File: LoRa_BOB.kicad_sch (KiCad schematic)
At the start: 8 parts, among them U1 1597-1488-ND, U2 XC6210B332MR-G, U3 74HC4050D

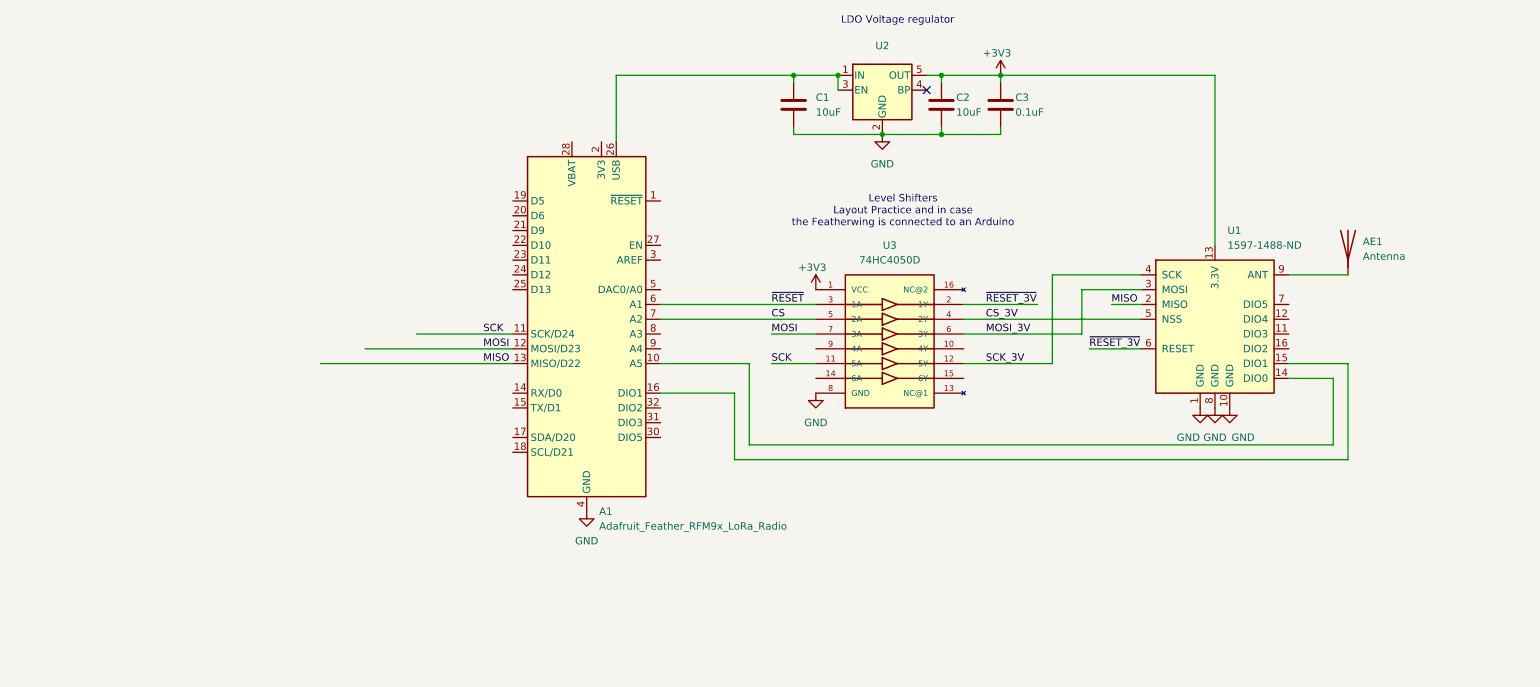
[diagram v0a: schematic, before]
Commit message: netclass directive cleanup
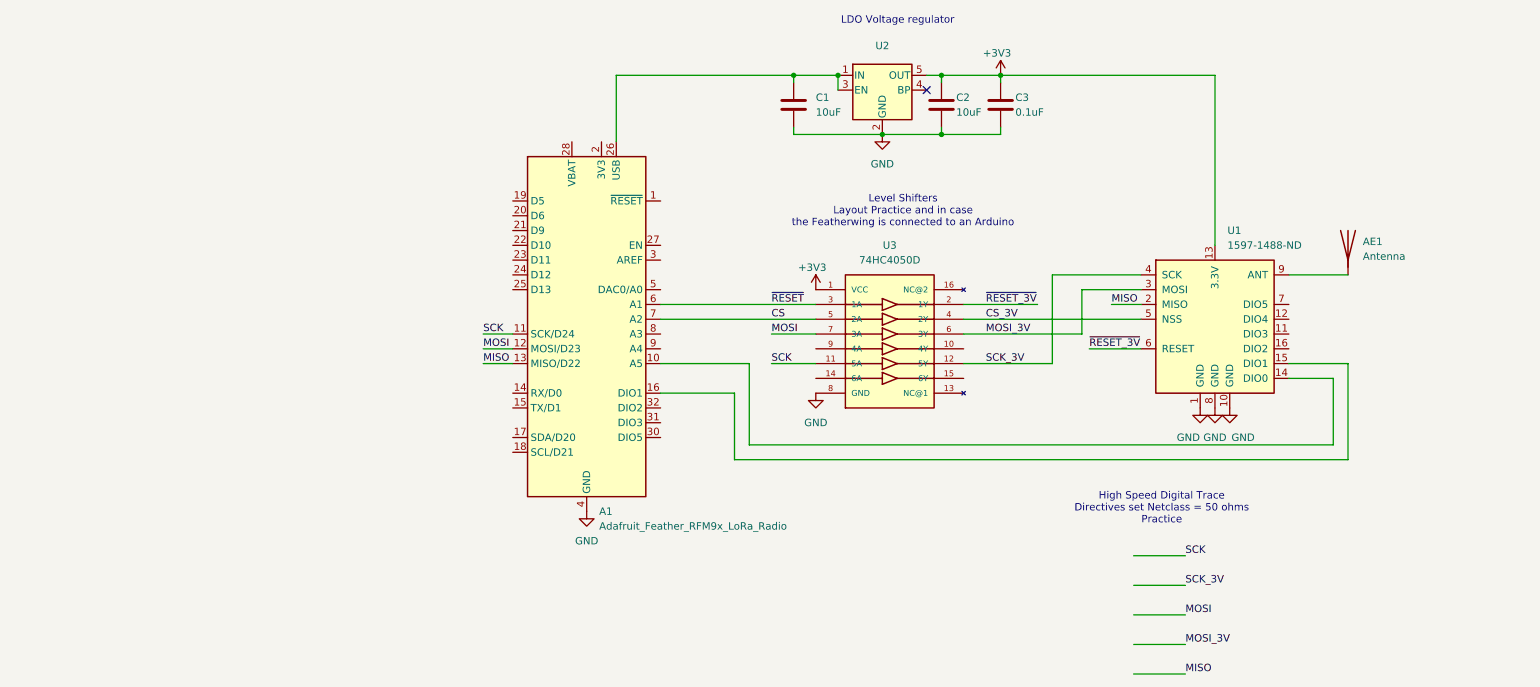
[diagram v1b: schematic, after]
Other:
- note added: "High Speed Digital Trace Directives set Netclass = 50 ohms Practice"
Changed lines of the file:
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@@
+		)
+	)
+	(text "High Speed Digital Trace\nDirectives set Netclass = 50 ohms\nPractice"
+		(exclude_from_sim no)
+		(at 270.256 154.432 0)
+		(effects
+			(font
+				(size 1.27 1.27)
+			)
 		)
 	)
@@
 	(wire
 		(pts
-			(xy 125.73 129.54) (xy 158.75 129.54)
+			(xy 153.67 124.46) (xy 158.75 124.46)
 		)
 		(stroke
@@
 	(wire
 		(pts
+			(xy 153.67 127) (xy 158.75 127)
+		)
+		(stroke
+			(width 0)
+			(type default)
+		)
+	)
+	(wire
+		(pts
 			(xy 299.72 143.51) (xy 299.72 132.08)
 		)
@@
 	(wire
 		(pts
-			(xy 133.35 127) (xy 158.75 127)
-		)
-		(stroke
-			(width 0)
-			(type default)
-		)
-	)
-	(wire
-		(pts
 			(xy 232.41 88.9) (xy 232.41 90.17)
 		)
@@
 	(wire
 		(pts
+			(xy 265.43 167.64) (xy 274.32 167.64)
+		)
+		(stroke
+			(width 0)
+			(type default)
+		)
+	)
+	(wire
+		(pts
 			(xy 242.57 90.17) (xy 232.41 90.17)
 		)
@@
 	(wire
 		(pts
+			(xy 265.43 172.72) (xy 274.32 172.72)
+		)
+		(stroke
+			(width 0)
+			(type default)
+		)
+	)
+	(wire
+		(pts
 			(xy 207.01 90.17) (xy 222.25 90.17)
 		)
@@
 	(wire
 		(pts
+			(xy 265.43 162.56) (xy 274.32 162.56)
+		)
+		(stroke
+			(width 0)
+			(type default)
+		)
+	)
+	(wire
+		(pts
 			(xy 236.22 119.38) (xy 248.92 119.38)
 		)
@@
 	(wire
 		(pts
+			(xy 153.67 129.54) (xy 158.75 129.54)
+		)
+		(stroke
+			(width 0)
+			(type default)
+		)
+	)
+	(wire
+		(pts
 			(xy 184.15 121.92) (xy 210.82 121.92)
 		)
@@
 	(wire
 		(pts
+			(xy 265.43 182.88) (xy 274.32 182.88)
+		)
+		(stroke
+			(width 0)
+			(type default)
+		)
+	)
+	(wire
+		(pts
 			(xy 176.53 91.44) (xy 176.53 80.01)
 		)
@@
 	(wire
 		(pts
-			(xy 142.24 124.46) (xy 158.75 124.46)
+			(xy 265.43 177.8) (xy 274.32 177.8)
 		)
 		(stroke
@@
 		)
 	)
+	(label "MOSI"
+		(at 274.32 172.72 0)
+		(effects
+			(font
+				(size 1.27 1.27)
+			)
+			(justify left bottom)
+		)
+	)
+	(label "SCK"
+		(at 274.32 162.56 0)
+		(effects
+			(font
+				(size 1.27 1.27)
+			)
+			(justify left bottom)
+		)
+	)
 	(label "~{RESET}"
 		(at 203.2 119.38 0)
@@
 		)
 	)
+	(label "MOSI_3V"
+		(at 274.32 177.8 0)
+		(effects
+			(font
+				(size 1.27 1.27)
+			)
+			(justify left bottom)
+		)
+	)
 	(label "CS_3V"
 		(at 240.03 121.92 0)
@@
 	)
 	(label "SCK_3V"
+		(at 274.32 167.64 0)
+		(effects
+			(font
+				(size 1.27 1.27)
+			)
+			(justify left bottom)
+		)
+	)
+	(label "MISO"
+		(at 274.32 182.88 0)
+		(effects
+			(font
+				(size 1.27 1.27)
+			)
+			(justify left bottom)
+		)
+	)
+	(label "SCK_3V"
 		(at 240.03 129.54 0)
 		(effects
@@
 			)
 			(justify left bottom)
-		)
-	)
-	(netclass_flag ""
-		(length 2.54)
-		(shape round)
-		(at 142.24 124.46 0)
-		(fields_autoplaced yes)
-		(effects
-			(font
-				(size 1.27 1.27)
-			)
-			(justify left bottom)
-		)
-		(property "Netclass" "50 ohm"
-			(at 142.9385 121.92 0)
-			(effects
-				(font
-					(size 1.27 1.27)
-				)
-				(justify left)
-			)
-		)
-		(property "Component Class" ""
-			(at -1.27 1.27 0)
-			(effects
-				(font
-					(size 1.27 1.27)
-					(italic yes)
-				)
-			)
-		)
-	)
-	(netclass_flag ""
-		(length 2.54)
-		(shape round)
-		(at 133.35 127 0)
-		(fields_autoplaced yes)
-		(effects
-			(font
-				(size 1.27 1.27)
-			)
-			(justify left bottom)
-		)
-		(property "Netclass" "50 ohm"
-			(at 134.0485 124.46 0)
-			(effects
-				(font
-					(size 1.27 1.27)
-				)
-				(justify left)
-			)
-		)
-		(property "Component Class" ""
-			(at -20.32 0 0)
-			(effects
-				(font
-					(size 1.27 1.27)
-					(italic yes)
-				)
-			)
 		)
 	)
@@
 		(length 2.54)
 		(shape round)
-		(at 254 114.3 0)
+		(at 265.43 182.88 0)
 		(fields_autoplaced yes)
 		(effects
@@
 		)
 		(property "Netclass" "50 ohm"
-			(at 254.6985 111.76 0)
+			(at 266.1285 180.34 0)
 			(effects
 				(font
@@
 		)
 		(property "Component Class" ""
-			(at 0 -10.16 0)
+			(at 120.65 54.61 0)
 			(effects
 				(font
@@
 		(length 2.54)
 		(shape round)
-		(at 125.73 129.54 0)
+		(at 265.43 172.72 0)
 		(fields_autoplaced yes)
 		(effects
@@
 		)
 		(property "Netclass" "50 ohm"
-			(at 126.4285 127 0)
+			(at 266.1285 170.18 0)
 			(effects
 				(font
@@
 		)
 		(property "Component Class" ""
-			(at -19.05 1.27 0)
+			(at 111.76 45.72 0)
 			(effects
 				(font
@@
 		(length 2.54)
 		(shape round)
-		(at 256.54 119.38 0)
+		(at 265.43 167.64 0)
 		(fields_autoplaced yes)
 		(effects
@@
 		)
 		(property "Netclass" "50 ohm"
-			(at 257.2385 116.84 0)
+			(at 266.1285 165.1 0)
 			(effects
 				(font
@@
 		)
 		(property "Component Class" ""
-			(at 2.54 -5.08 0)
+			(at 120.65 39.37 0)
 			(effects
 				(font
@@
 		(length 2.54)
 		(shape round)
-		(at 246.38 129.54 0)
+		(at 265.43 162.56 0)
 		(fields_autoplaced yes)
 		(effects
@@
 		)
 		(property "Netclass" "50 ohm"
-			(at 247.0785 127 0)
+			(at 266.1285 160.02 0)
 			(effects
 				(font
@@
 		)
 		(property "Component Class" ""
-			(at -1.27 0 0)
+			(at 121.92 39.37 0)
 			(effects
 				(font
+					(size 1.27 1.27)
+					(italic yes)
+				)
+			)
+		)
+	)
+	(netclass_flag ""
+		(length 2.54)
+		(shape round)
+		(at 265.43 177.8 0)
+		(fields_autoplaced yes)
+		(effects
+			(font
+				(size 1.27 1.27)
+			)
+			(justify left bottom)
+		)
+		(property "Netclass" "50 ohm"
+			(at 266.1285 175.26 0)
+			(effects
+				(font
+					(size 1.27 1.27)
+				)
+				(justify left)
+			)
+		)
+		(property "Component Class" ""
+			(at 120.65 49.53 0)
+			(effects
+				(font

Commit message: better routing
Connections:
- no-connect marks 1 -> 9
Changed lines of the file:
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@@
+	)
+	(no_connect
+		(at 292.1 127)
+	)
+	(no_connect
+		(at 292.1 124.46)
+	)
+	(no_connect
+		(at 210.82 127)
+	)
+	(no_connect
+		(at 292.1 119.38)
 	)
 	(no_connect
 		(at 229.87 82.55)
 	)
+	(no_connect
+		(at 236.22 132.08)
+	)
+	(no_connect
+		(at 210.82 132.08)
+	)
+	(no_connect
+		(at 236.22 127)
+	)
+	(no_connect
+		(at 292.1 121.92)
+	)
 	(wire
 		(pts
@@
 	(wire
 		(pts
-			(xy 236.22 119.38) (xy 248.92 119.38)
-		)
-		(stroke
-			(width 0)
-			(type default)
-		)
-	)
-	(wire
-		(pts
 			(xy 203.2 129.54) (xy 210.82 129.54)
 		)
@@
 		)
 		(stroke
+			(width 0)
+			(type default)
+		)
+	)
+	(wire
+		(pts
+			(xy 236.22 119.38) (xy 240.03 119.38)
+		)
+		(stroke

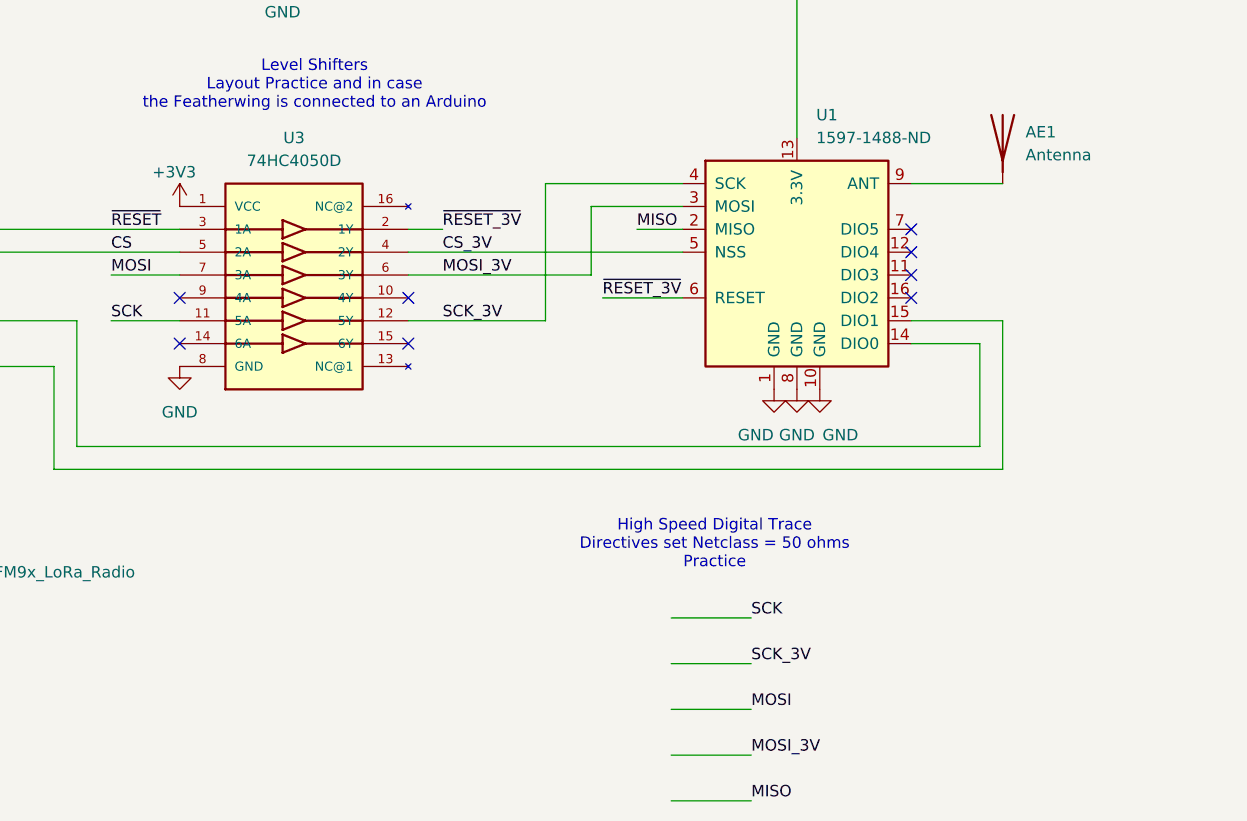
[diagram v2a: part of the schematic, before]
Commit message: Better netclasses and 50 ohm trace widths
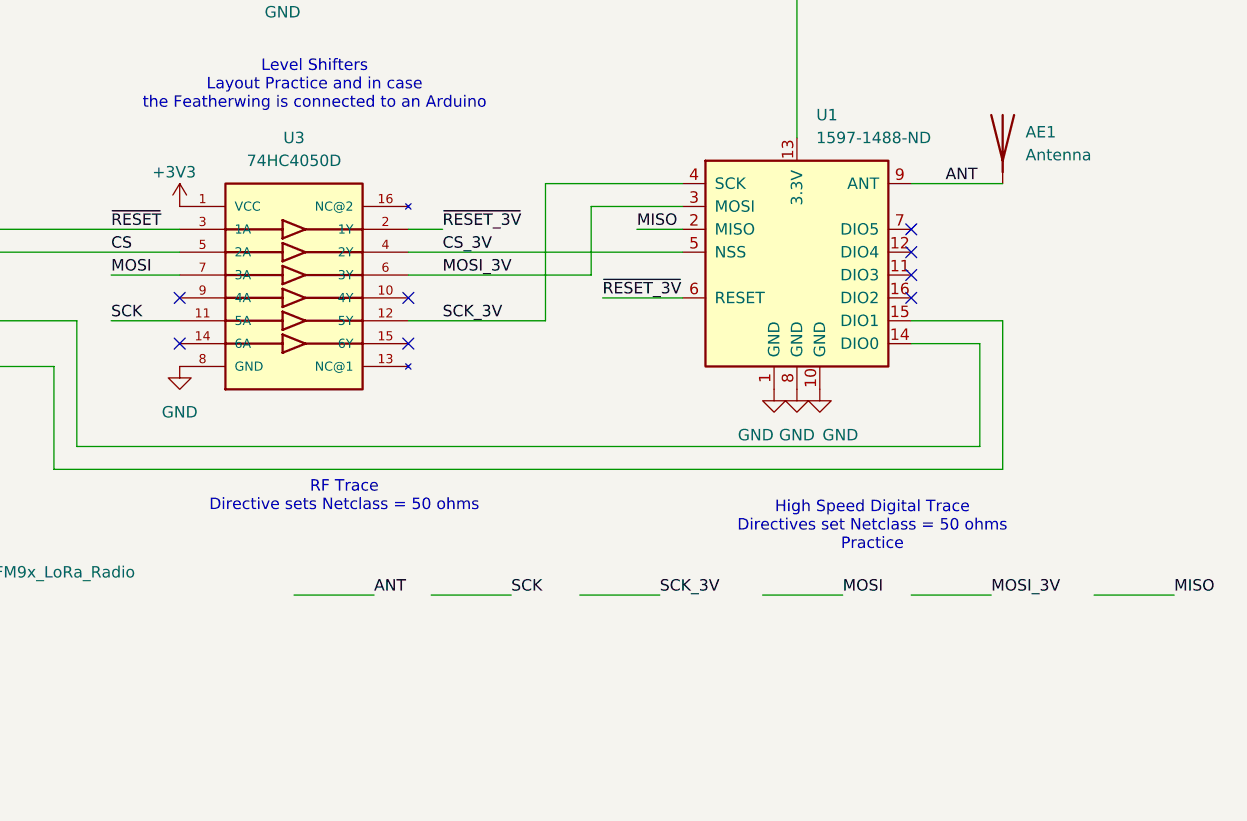
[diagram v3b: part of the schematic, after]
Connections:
- net ANT: now reaches AE1.1 (A), U1.9 (ANT)
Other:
- note added: "RF Trace Directive sets Netclass = 50 ohms"
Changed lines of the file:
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@@
 	(text "High Speed Digital Trace\nDirectives set Netclass = 50 ohms\nPractice"
 		(exclude_from_sim no)
-		(at 270.256 154.432 0)
+		(at 287.782 152.4 0)
+		(effects
+			(font
+				(size 1.27 1.27)
+			)
+		)
+	)
+	(text "RF Trace\nDirective sets Netclass = 50 ohms"
+		(exclude_from_sim no)
+		(at 229.108 149.098 0)
 		(effects
 			(font
@@
 	(wire
 		(pts
+			(xy 223.52 160.02) (xy 232.41 160.02)
+		)
+		(stroke
+			(width 0)
+			(type default)
+		)
+	)
+	(wire
+		(pts
 			(xy 232.41 88.9) (xy 232.41 90.17)
 		)
@@
 	(wire
 		(pts
-			(xy 265.43 167.64) (xy 274.32 167.64)
+			(xy 255.27 160.02) (xy 264.16 160.02)
 		)
 		(stroke
@@
 	(wire
 		(pts
-			(xy 265.43 172.72) (xy 274.32 172.72)
+			(xy 275.59 160.02) (xy 284.48 160.02)
 		)
 		(stroke
@@
 	(wire
 		(pts
-			(xy 265.43 162.56) (xy 274.32 162.56)
+			(xy 238.76 160.02) (xy 247.65 160.02)
 		)
 		(stroke
@@
 	(wire
 		(pts
-			(xy 265.43 182.88) (xy 274.32 182.88)
+			(xy 312.42 160.02) (xy 321.31 160.02)
 		)
 		(stroke
@@
 	(wire
 		(pts
-			(xy 265.43 177.8) (xy 274.32 177.8)
+			(xy 292.1 160.02) (xy 300.99 160.02)
 		)
 		(stroke
@@
 	)
 	(label "MOSI"
-		(at 274.32 172.72 0)
+		(at 284.48 160.02 0)
 		(effects
 			(font
@@
 	)
 	(label "SCK"
-		(at 274.32 162.56 0)
+		(at 247.65 160.02 0)
+		(effects
+			(font
+				(size 1.27 1.27)
+			)
+			(justify left bottom)
+		)
+	)
+	(label "ANT"
+		(at 232.41 160.02 0)
 		(effects
 			(font
@@
 		)
 	)
+	(label "ANT"
+		(at 295.91 114.3 0)
+		(effects
+			(font
+				(size 1.27 1.27)
+			)
+			(justify left bottom)
+		)
+	)
 	(label "~{RESET_3V}"
 		(at 257.81 127 0)
@@
 	)
 	(label "MOSI_3V"
-		(at 274.32 177.8 0)
+		(at 300.99 160.02 0)
 		(effects
 			(font
@@
 	)
 	(label "SCK_3V"
-		(at 274.32 167.64 0)
+		(at 264.16 160.02 0)
 		(effects
 			(font
@@
 	)
 	(label "MISO"
-		(at 274.32 182.88 0)
+		(at 321.31 160.02 0)
 		(effects
 			(font
@@
 		(length 2.54)
 		(shape round)
-		(at 295.91 114.3 0)
+		(at 223.52 160.02 0)
 		(fields_autoplaced yes)
 		(effects
@@
 		)
 		(property "Netclass" "50 ohm"
-			(at 296.6085 111.76 0)
+			(at 224.2185 157.48 0)
 			(effects
 				(font
@@
 		)
 		(property "Component Class" ""
-			(at -200.66 -34.29 0)
+			(at 78.74 31.75 0)
 			(effects
 				(font
@@
 		(length 2.54)
 		(shape round)
-		(at 265.43 182.88 0)
+		(at 312.42 160.02 0)
 		(fields_autoplaced yes)
 		(effects
@@
 		)
 		(property "Netclass" "50 ohm"
-			(at 266.1285 180.34 0)
+			(at 313.1185 157.48 0)
 			(effects
 				(font
@@
 		)
 		(property "Component Class" ""
-			(at 120.65 54.61 0)
+			(at 167.64 31.75 0)
 			(effects
 				(font
@@
 		(length 2.54)
 		(shape round)
-		(at 265.43 172.72 0)
+		(at 275.59 160.02 0)
 		(fields_autoplaced yes)
 		(effects
@@
 		)
 		(property "Netclass" "50 ohm"
-			(at 266.1285 170.18 0)
+			(at 276.2885 157.48 0)
 			(effects
 				(font
@@
 		)
 		(property "Component Class" ""
-			(at 111.76 45.72 0)
+			(at 121.92 33.02 0)
 			(effects
 				(font
@@
 		(length 2.54)
 		(shape round)
-		(at 265.43 167.64 0)
+		(at 255.27 160.02 0)
 		(fields_autoplaced yes)
 		(effects
@@
 		)
 		(property "Netclass" "50 ohm"
-			(at 266.1285 165.1 0)
+			(at 255.9685 157.48 0)
 			(effects
 				(font
@@
 		)
 		(property "Component Class" ""
-			(at 120.65 39.37 0)
+			(at 110.49 31.75 0)
 			(effects
 				(font
@@
 		(length 2.54)
 		(shape round)
-		(at 265.43 162.56 0)
+		(at 238.76 160.02 0)
 		(fields_autoplaced yes)
 		(effects
@@
 		)
 		(property "Netclass" "50 ohm"
-			(at 266.1285 160.02 0)
+			(at 239.4585 157.48 0)
 			(effects
 				(font
@@
 		)
 		(property "Component Class" ""
-			(at 121.92 39.37 0)
+			(at 95.25 36.83 0)
 			(effects
 				(font
@@
 		(length 2.54)
 		(shape round)
-		(at 265.43 177.8 0)
+		(at 292.1 160.02 0)
 		(fields_autoplaced yes)
 		(effects
@@
 		)
 		(property "Netclass" "50 ohm"
-			(at 266.1285 175.26 0)
+			(at 292.7985 157.48 0)
 			(effects
 				(font
@@
 		)
 		(property "Component Class" ""
-			(at 120.65 49.53 0)
+			(at 147.32 31.75 0)
 			(effects
 				(font

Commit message: LEDs
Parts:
- added D1, D3: LED, LED_SMD:LED_0603_1608Metric_Pad1.05x0.95mm_HandSolder, symbol Device:LED
- added D2: SML-D12D8WT86, LED_SMD:LED_0603_1608Metric_Pad1.05x0.95mm_HandSolder, symbol Device:LED
- added R1, R2, R3: 1K, Resistor_SMD:R_0201_0603Metric_Pad0.64x0.40mm_HandSolder, symbol Device:R_US
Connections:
- net +3V3: now also D1.2 (A)
- net GND: now also R1.2, R2.2, R3.2
- net ORANGE: now reaches A1.19 (D5)
- net ORANGE: now also D2.2 (A)
- net YELLOW: now reaches A1.20 (D6)
- net YELLOW: now also D3.2 (A)
- new net: D2.1 (K), R2.1
- new net: D3.1 (K), R3.1
- new net: D1.1 (K), R1.1
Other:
- note added: "POWER"
- note added: "RX"
- note added: "TX"
